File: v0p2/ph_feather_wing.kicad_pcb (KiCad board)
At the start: 2 copper layers, 22.9 x 50.8 mm, 14 parts, among them J1 Conn_Coaxial, J2 Screw_Terminal_01x03, SW1 SW_Push, SW2 SW_Push, U1 LMP7721, U2 LMP7721

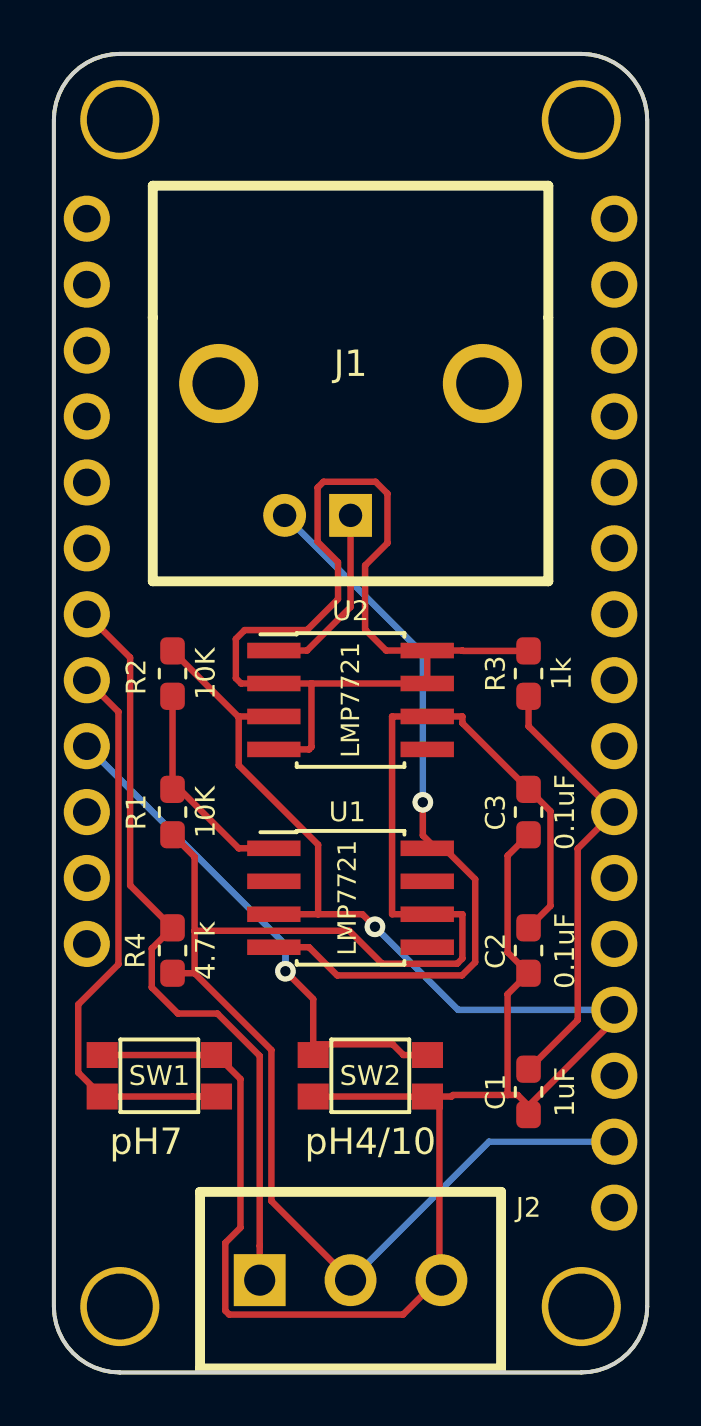
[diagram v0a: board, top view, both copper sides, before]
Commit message: Finished preliminary draft of version 0.2 R1.
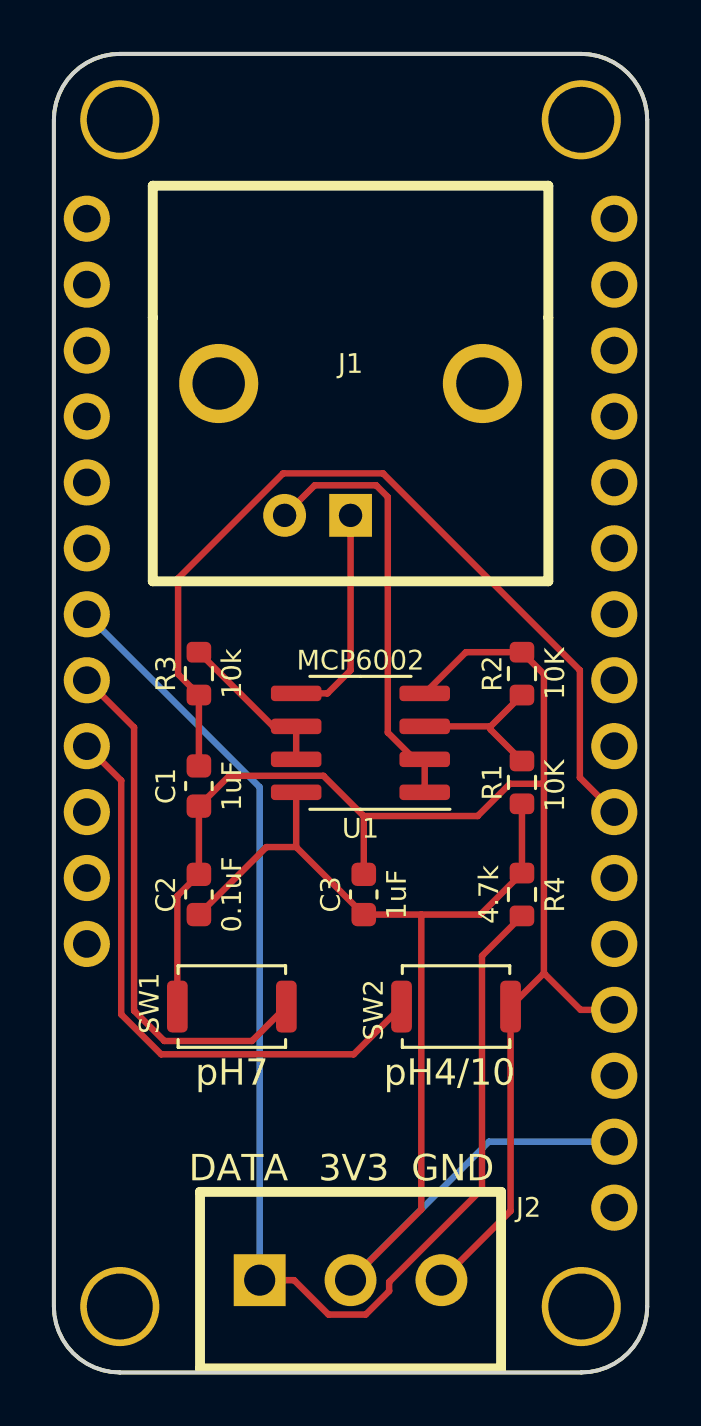
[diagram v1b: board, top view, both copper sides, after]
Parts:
- removed U2: LMP7721, SOIC-8_3.9x4.9mm_P1.27mm_HandSolder:SOIC-8_3.9x4.9mm_P1.27mm_HandSolder
- C1, C2: footprint Capacitor_SMD:C_0603_1608Metric_Pad1.05x0.95mm_HandSolder -> Capacitor_SMD:C_0603_1608Metric
- C3: value 0.1uF -> 1uF; footprint Capacitor_SMD:C_0603_1608Metric_Pad1.05x0.95mm_HandSolder -> Capacitor_SMD:C_0603_1608Metric
- R1, R2, R4: footprint Resistor_SMD:R_0603_1608Metric_Pad1.05x0.95mm_HandSolder -> Resistor_SMD:R_0603_1608Metric
- R3: value 1k -> 10k; footprint Resistor_SMD:R_0603_1608Metric_Pad1.05x0.95mm_HandSolder -> Resistor_SMD:R_0603_1608Metric
- SW1, SW2: footprint KMR7_SWITCH:KMR7_SWITCH -> Button_Switch_SMD:SW_Push_SPST_NO_Alps_SKRK
- U1: value LMP7721 -> MCP6002; footprint SOIC-8_3.9x4.9mm_P1.27mm_HandSolder:SOIC-8_3.9x4.9mm_P1.27mm_HandSolder -> Package_SO:SOIC-8_3.9x4.9mm_P1.27mm
- moved C1 17.3 mm to (70.4, 79.0)
- moved R4 13.6 mm to (82.8, 83.2), turned to 270 degrees
- moved R1 13.5 mm to (82.8, 78.9)
- moved R2 13.5 mm to (82.8, 74.7)
- moved C2 12.9 mm to (70.4, 83.2), turned to 90 degrees
- moved R3 12.7 mm to (70.4, 74.7), turned to 90 degrees
- moved C3 7.10 mm to (76.7, 83.2), turned to 90 degrees
- moved U1 5.98 mm to (76.6, 77.3), turned to 180 degrees
- moved SW2 4.24 mm to (80.3, 87.5)
- moved SW1 3.86 mm to (71.6, 87.5)
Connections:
- R3 pad 1: Net-(R3-Pad1) -> /PH_VOUT
- R3 pad 2: /PH_VOUT -> Net-(R3-Pad2)
- U1 pad 1: Net-(R1-Pad2) -> /PROBE_VGND
- U1 pad 2: Net-(U1-Pad2) -> /PROBE_VGND
- U1 pad 3: GND -> Net-(R1-Pad2)
- U1 pad 4: /PROBE_VGND -> GND
- U1 pad 5: Net-(U1-Pad5) -> /PROBE_OUT
- U1 pad 6: /3V3 -> Net-(R3-Pad2)
- U1 pad 7: Net-(U1-Pad7) -> Net-(R3-Pad2)
- U1 pad 8: /PROBE_VGND -> /3V3
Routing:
- net Net-(R3-Pad1): track 38.6 -> 0.00 mm
- net GND: track 84.3 -> 59.1 mm, vias 1 -> 0
- net /3V3: track 68.8 -> 47.6 mm
- net /TEMP_DATA: track 30.0 -> 50.9 mm
- net /PH_VOUT: track 17.1 -> 33.9 mm
- net /PROBE_VGND: track 29.2 -> 16.8 mm, vias 1 -> 0
- net Net-(R3-Pad2): track 0.00 -> 6.20 mm
- net /BUTTON_2: track 20.1 -> 23.1 mm, vias 1 -> 0
- net Net-(R1-Pad2): track 8.43 -> 6.08 mm
- net /BUTTON_1: track 22.0 -> 20.4 mm
- net /PROBE_OUT: track 7.18 -> 8.43 mm
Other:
- board text added: "3V3"
- board text added: "DATA"
- board text added: "GND"
- board text added: "pH Feather Wing V0.2 R1 www.iorodeo.com"
- board text removed: "pH Feather Wing V0.1 R1 www.iorodeo.com"

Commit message: Added guard ring, re-routed, made r1 gerbers, added files for assembly.
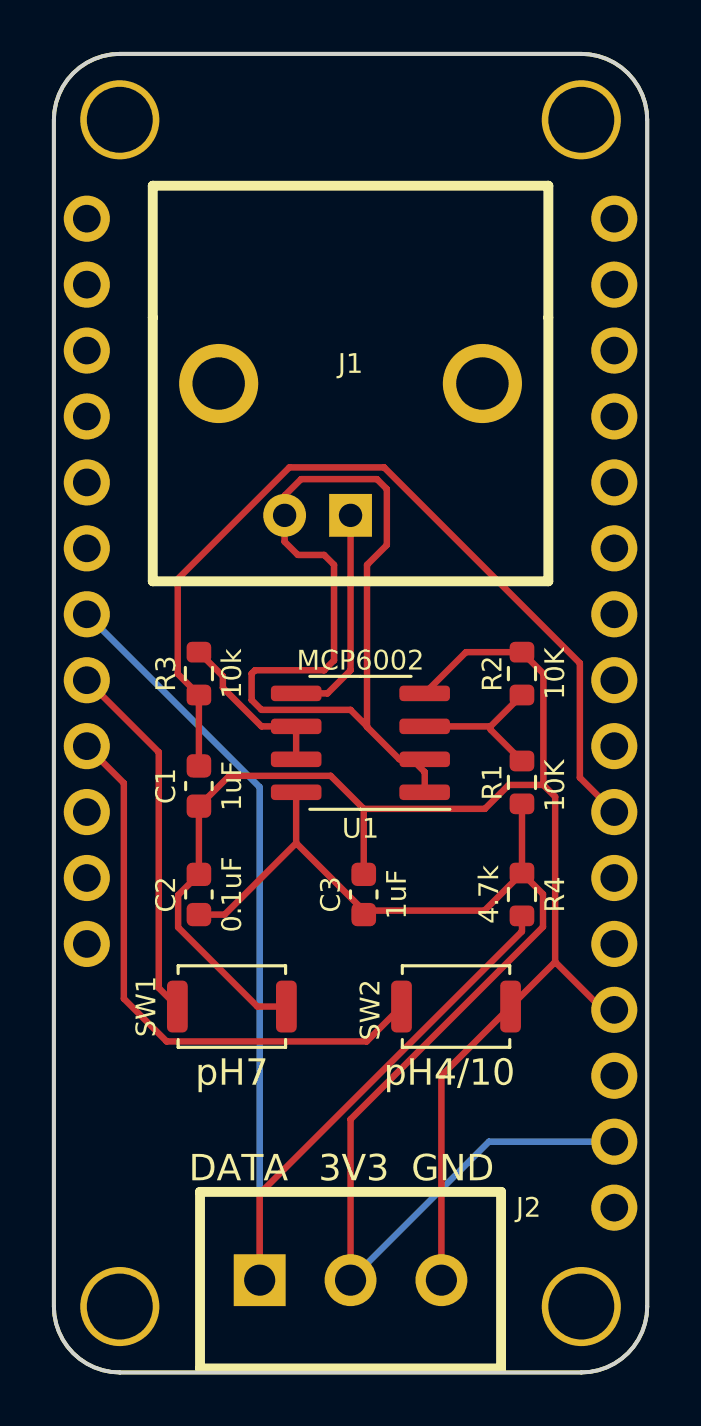
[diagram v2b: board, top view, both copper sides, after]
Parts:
- turned SW1 to 0 degrees
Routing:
- net /PROBE_VGND: track 16.8 -> 35.1 mm
- net /BUTTON_1: track 20.4 -> 14.0 mm
- net /TEMP_DATA: track 50.9 -> 46.6 mm
- net /3V3: track 47.6 -> 51.5 mm
- net GND: track 59.1 -> 61.6 mm
- net /BUTTON_2: track 23.1 -> 22.3 mm
